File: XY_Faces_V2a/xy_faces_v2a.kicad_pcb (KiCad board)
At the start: 4 copper layers, 83 x 98 mm, 33 parts, among them CN1 DF13A-5P-1.25H(21), CN2 DF13C-5P-1.25V(21), J2 Conn_01x01, J3 Conn_01x01, J4 Conn_01x01, J5 Conn_01x01, U1 VEML7700, U2 MCP9808_DFN, U3 DRV2605LDGS

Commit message: minor changes
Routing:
- net GND: track 94.2 -> 87.1 mm, vias 12 -> 11
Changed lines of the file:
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@@
-	)
-	(via
-		(at 143 127)
-		(size 0.8)
-		(drill 0.4)
-		(layers "F.Cu" "B.Cu")
-		(net 1)
 	)
 	(via
@@
 	)
 	(segment
-		(start 143 130.8)
-		(end 143.35 131.15)
-		(width 0.5)
-		(layer "B.Cu")
-		(net 1)
-	)
-	(segment
 		(start 151.25 119.975)
 		(end 149.75 119.975)
@@
 	)
 	(segment
-		(start 143.35 133.9)
-		(end 143.3 133.95)
-		(width 0.5)
-		(layer "B.Cu")
-		(net 1)
-	)
-	(segment
-		(start 143 127)
-		(end 143 130.8)
-		(width 0.5)
-		(layer "B.Cu")
-		(net 1)
-	)
-	(segment
 		(start 146.225 119.95)
 		(end 146.2 119.975)
-		(width 0.5)
-		(layer "B.Cu")
-		(net 1)
-	)
-	(segment
-		(start 143.35 131.15)
-		(end 143.35 133.9)
 		(width 0.5)
 		(layer "B.Cu")
@@
 	)
 	(segment
-		(start 144.6 134.1)
-		(end 144.45 133.95)
-		(width 0.5)
-		(layer "B.Cu")
-		(net 2)
-	)
-	(segment
 		(start 139.975 114.25)
 		(end 137.825 114.25)
@@
 		(start 148.7 110.3)
 		(end 151.825 113.425)
-		(width 0.5)
-		(layer "B.Cu")
-		(net 2)
-	)
-	(segment
-		(start 144.5 133.9)
-		(end 144.55 133.95)
 		(width 0.5)
 		(layer "B.Cu")
@@
 	)
 	(segment
-		(start 142 134)
-		(end 142.1 134.1)
-		(width 0.5)
-		(layer "B.Cu")
-		(net 3)
-	)
-	(segment
 		(start 139.9 117.65)
 		(end 139.9 116.25)
@@
 		(width 0.25)
 		(layer "F.Cu")
-		(net 8)
-	)
-	(segment
-		(start 147.05 133.95)
-		(end 147 133.9)
-		(width 0.5)
-		(layer "B.Cu")
 		(net 8)
 	)
@@
 		(net 9)
 	)
-	(segment
-		(start 145.8 133.95)
-		(end 145.75 133.9)
-		(width 0.5)
-		(layer "B.Cu")
-		(net 9)
-	)

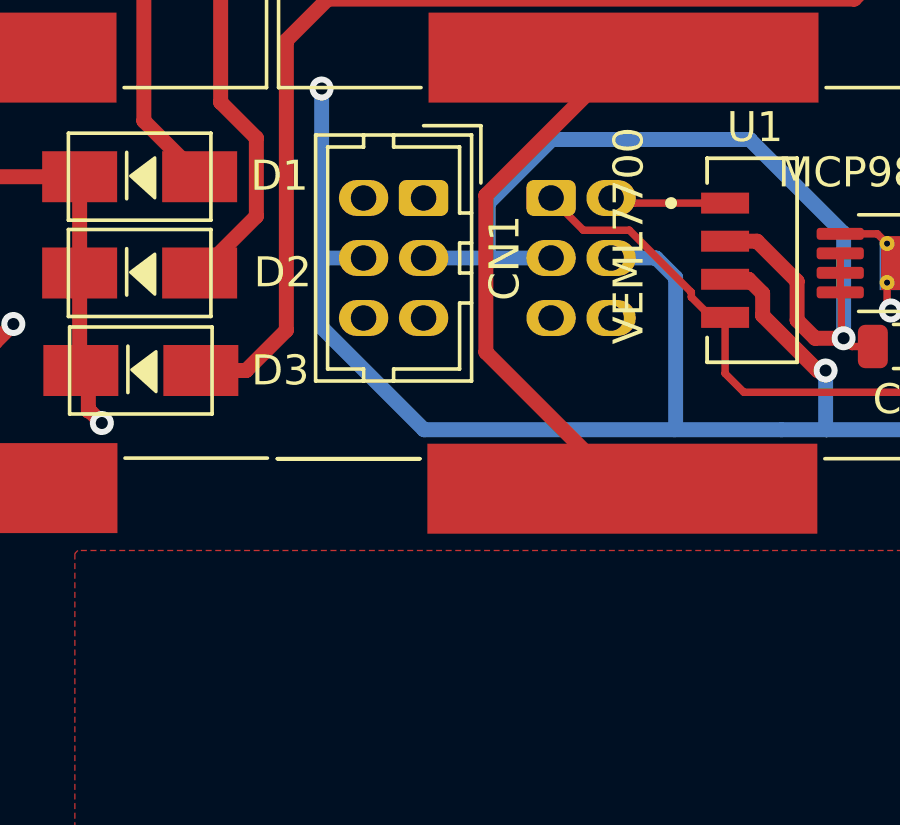
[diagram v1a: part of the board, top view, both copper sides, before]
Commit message: Added TCA Buffer
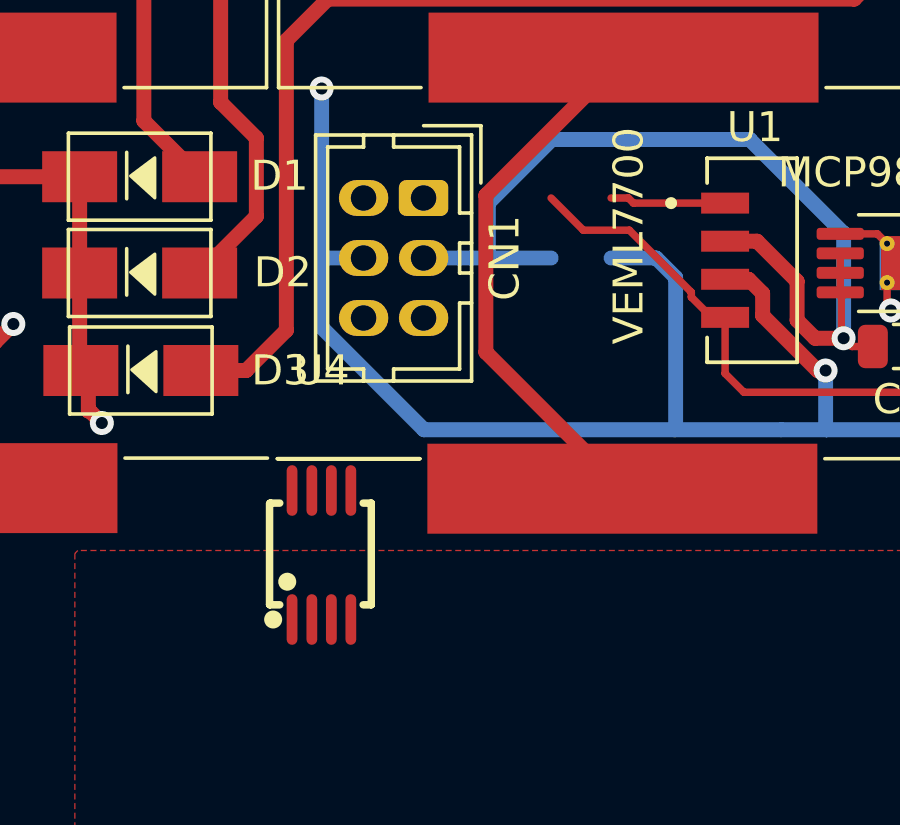
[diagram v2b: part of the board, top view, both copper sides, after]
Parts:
- removed CN2: DF13C-5P-1.25V(21), Connector_Hirose:Hirose_DF11-6DP-2DSA_2x03_P2.00mm_Vertical
- added U4: TCA4311ADGKR, easyeda2kicad:MSOP-8_L3.0-W3.0-P0.65-LS5.0-BL, F.Cu at (134.4, 124.2)
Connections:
- CN1 pad 1: SDA -> unconnected-(CN1-Pin_1-Pad1)
- CN1 pad 2: SCL -> unconnected-(CN1-Pin_2-Pad2)
- CN1 pad 3: +3V3 -> unconnected-(CN1-Pin_3-Pad3)
- CN1 pad 4: GND -> unconnected-(CN1-Pin_4-Pad4)
- CN1 pad 5: VSOLAR -> unconnected-(CN1-Pin_5-Pad5)
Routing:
- net unconnected-(CN1-Pin_1-Pad1): track 0.00 -> 4.25 mm
- net SDA: track 28.4 -> 24.2 mm

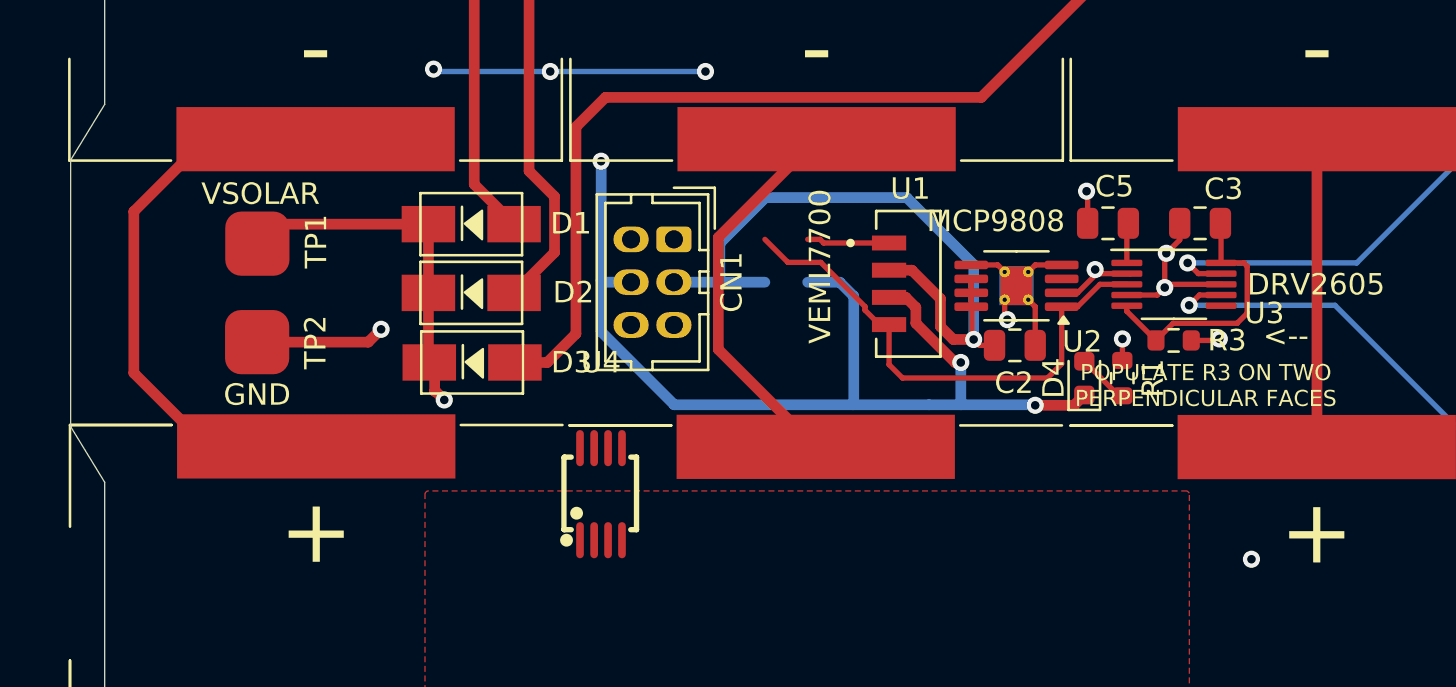
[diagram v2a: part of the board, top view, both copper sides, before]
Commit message: Rewired Face
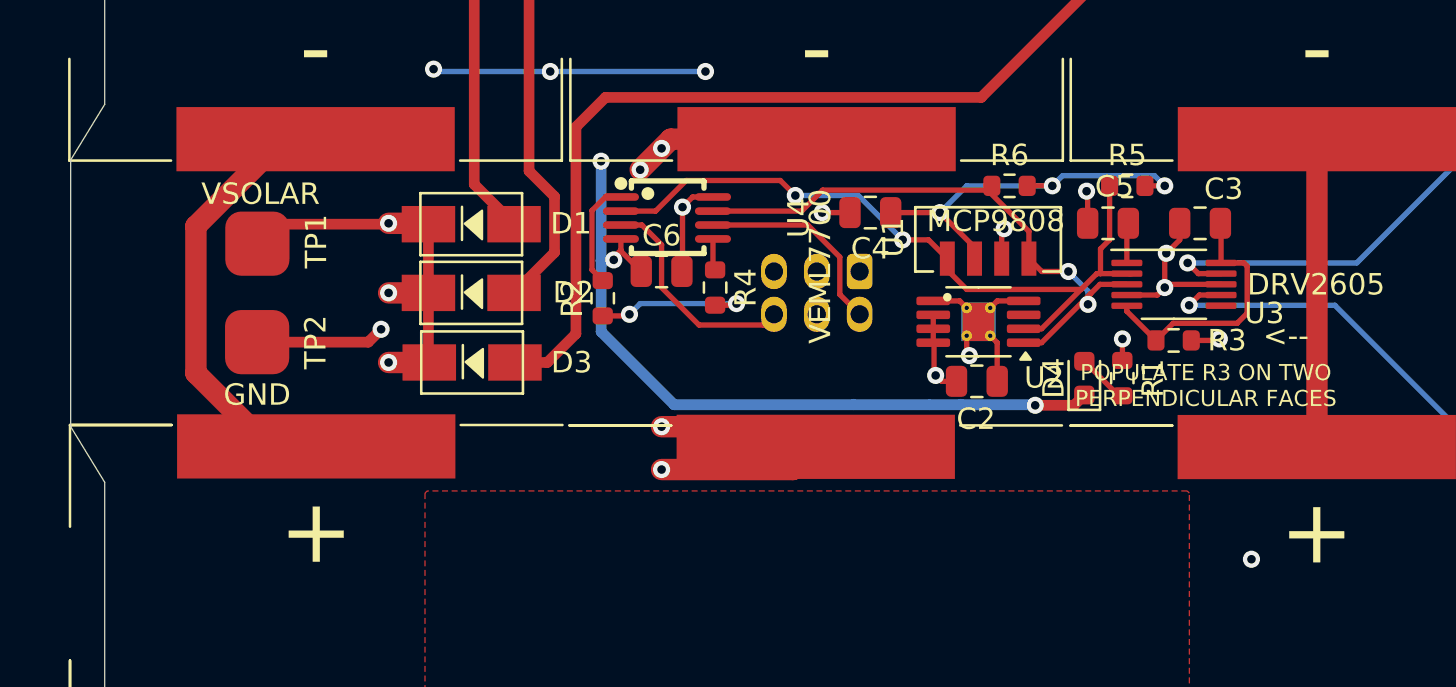
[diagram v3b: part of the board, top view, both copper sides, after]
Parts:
- added C4: 100nF, Capacitor_SMD:C_0805_2012Metric, F.Cu at (147.0, 111.0)
- added C6: 100nF, Capacitor_SMD:C_0805_2012Metric, F.Cu at (137.2, 113.8)
- added R2: 10k, Resistor_SMD:R_0603_1608Metric, F.Cu at (134.5, 115.0)
- added R4: 10k, Resistor_SMD:R_0603_1608Metric, F.Cu at (139.8, 114.5)
- added R5: 10k, Resistor_SMD:R_0603_1608Metric, F.Cu at (159.0, 109.8)
- added R6: 10k, Resistor_SMD:R_0603_1608Metric, F.Cu at (153.5, 109.8)
- C2, C3: value 1uF -> 100nF
- CN1: value DF13A-5P-1.25H(21) -> DF11-2DSA-4DP; moved to B.Cu
- moved U4 13.3 mm to (137.5, 111.2), turned to -90 degrees
- moved CN1 8.80 mm to (146.5, 113.8), turned to 180 degrees
- moved U1 4.26 mm to (152.5, 112.2), turned to 90 degrees
- moved C2 2.44 mm to (152.0, 118.9)
- moved U2 2.44 mm to (152.1, 116.1)
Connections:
- CN1 pad 1: unconnected-(CN1-Pin_1-Pad1) -> GND
- CN1 pad 2: unconnected-(CN1-Pin_2-Pad2) -> Net-(CN1-Pin_2)
- CN1 pad 3: unconnected-(CN1-Pin_3-Pad3) -> VSOLAR
- CN1 pad 4: unconnected-(CN1-Pin_4-Pad4) -> +3V3
- CN1 pad 5: unconnected-(CN1-Pin_5-Pad5) -> VSOLAR
- CN1 pad 6: unconnected-(CN1-Pin_6-Pad6) -> Net-(CN1-Pin_6)
- U4 pad 1: unconnected-(U4-EN-Pad1) -> Net-(U4-EN)
- U4 pad 2: unconnected-(U4-SCLOUT-Pad2) -> SCL
- U4 pad 3: unconnected-(U4-SCLIN-Pad3) -> Net-(CN1-Pin_6)
- U4 pad 4: unconnected-(U4-GND-Pad4) -> GND
- U4 pad 5: unconnected-(U4-READY-Pad5) -> Net-(U4-READY)
- U4 pad 6: unconnected-(U4-SDAIN-Pad6) -> Net-(CN1-Pin_2)
- U4 pad 7: unconnected-(U4-SDAOUT-Pad7) -> SDA
- U4 pad 8: unconnected-(U4-VCC-Pad8) -> +3V3
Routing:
- net Net-(SC3--): track 18.2 -> 39.9 mm, vias 0 -> 4
- net +3V3: track 59.7 -> 76.9 mm, vias 6 -> 12
- net VSOLAR: track 36.3 -> 48.4 mm, vias 1 -> 3
- net Net-(CN1-Pin_6): track 0.00 -> 10.5 mm
- net GND: track 87.1 -> 77.2 mm, vias 11 -> 13
- net Net-(CN1-Pin_2): track 0.00 -> 9.60 mm
- net Net-(U4-EN): track 0.00 -> 5.09 mm
- net SCL: track 32.0 -> 36.4 mm, vias 1 -> 2
- net unconnected-(CN1-Pin_1-Pad1): track 4.25 -> 0.00 mm
- net SDA: track 24.2 -> 27.7 mm, vias 0 -> 2
- net Net-(U4-READY): track 0.00 -> 1.49 mm
- net Net-(SC1--): track 27.4 -> 26.3 mm

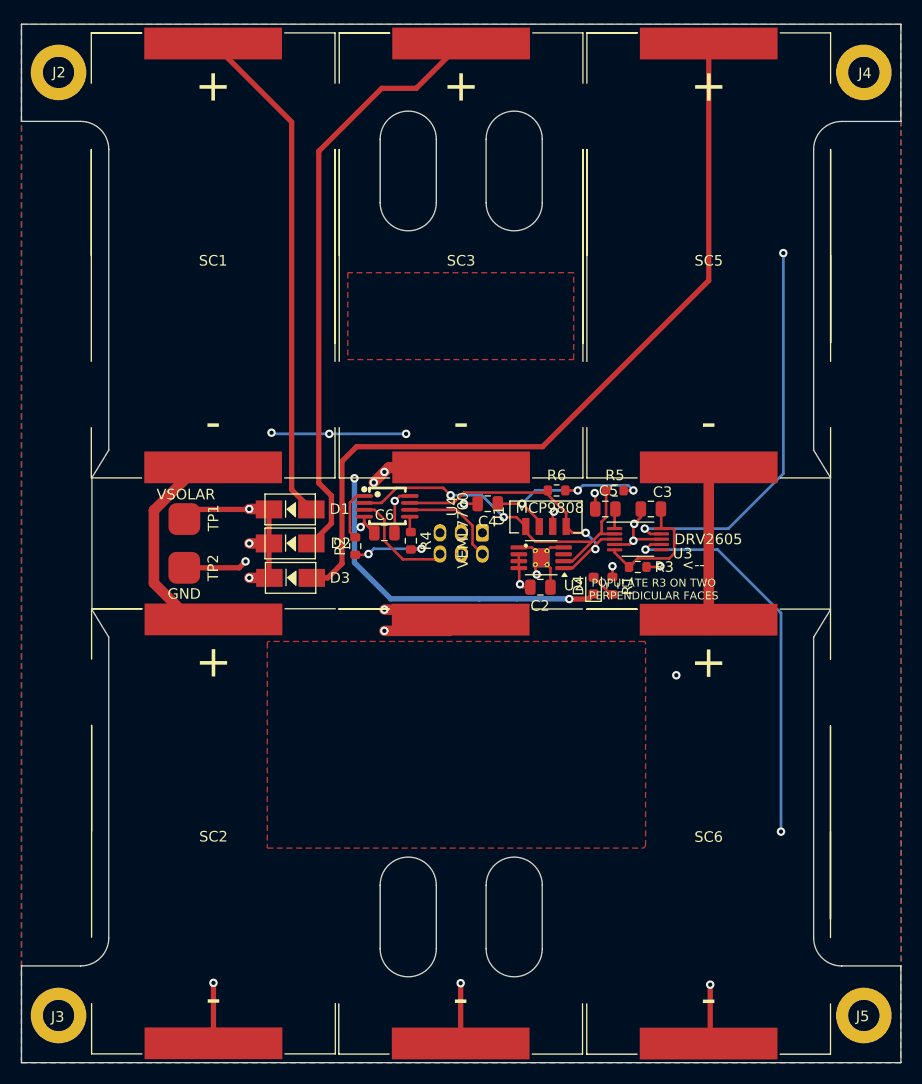
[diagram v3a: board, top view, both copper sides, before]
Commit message: Changed Mounting Holes to ISO M3
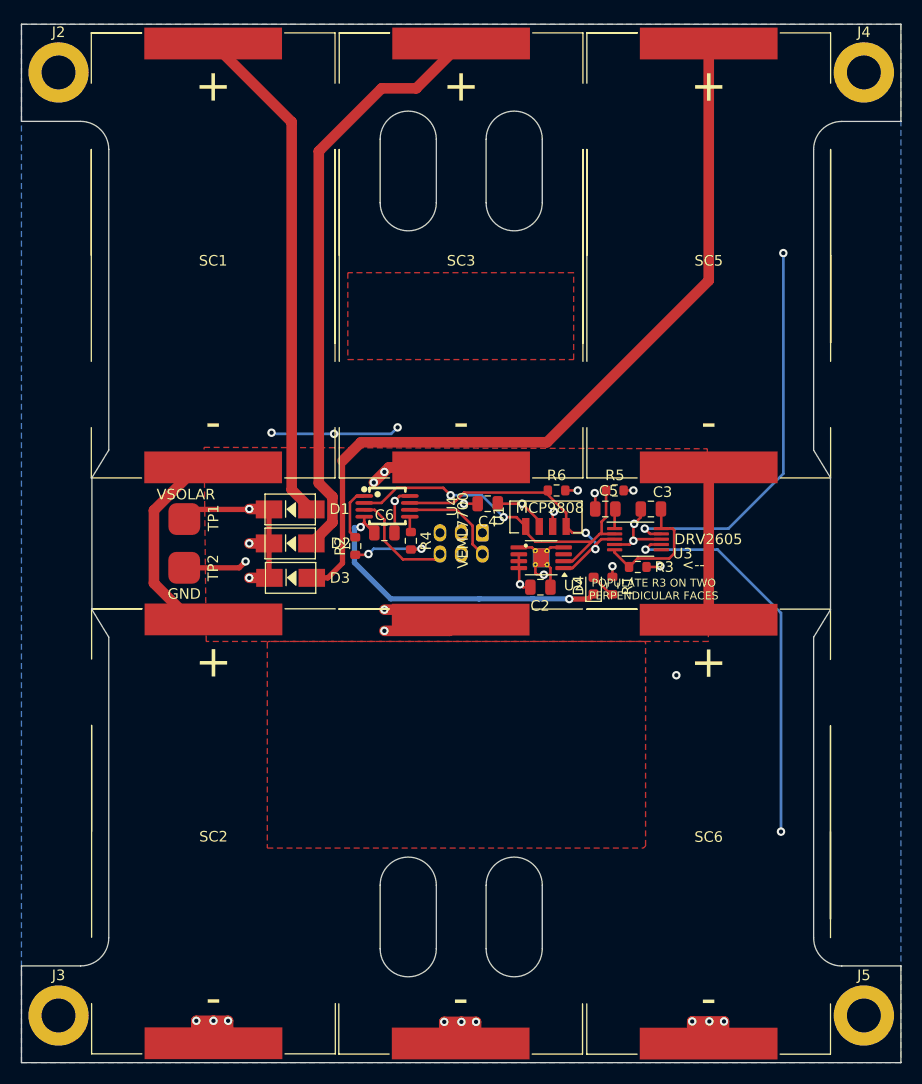
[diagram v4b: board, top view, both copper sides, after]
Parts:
- J2, J3, J4, J5: footprint SolarPanelBoards:MountingHoles -> MountingHole:MountingHole_3.2mm_M3_ISO7380_Pad
- moved J2 0.50 mm to (106.5, 70.3)
- moved J3 0.50 mm to (106.5, 159.3)
- moved J4 0.50 mm to (182.5, 70.3)
- moved J5 0.50 mm to (182.5, 159.3)
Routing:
- net +3V3: track 76.9 -> 101.7 mm
- net GND: track 77.2 -> 97.8 mm, vias 13 -> 18
- net Net-(SC1--): track 26.3 -> 21.2 mm
- net SCL: track 36.4 -> 34.8 mm
- added copper zone on In2.Cu, net +3V3
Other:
- board text added: "PROVES XY SOLAR: KIT V3 AMANDA EWING, NICOLE MAGGARD Rachel Rakushkin, Michael Pham"
- board text removed: "3V3"
- board text removed: "PROVES XY SOLAR: KIT V3 AMANDA EWING, NICOLE MAGGARD, Michael Pham"
- board text removed: "SCL"
- board text removed: "SDA"

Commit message: Generated Production Files
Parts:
- C2, C3, C4, C6: footprint Capacitor_SMD:C_0805_2012Metric -> Capacitor_SMD:C_0603_1608Metric
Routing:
- net +3V3: track 101.7 -> 82.4 mm, vias 12 -> 9
